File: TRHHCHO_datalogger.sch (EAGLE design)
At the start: 39 parts, among them J6 AMP FCI 10103594-0001LF, U1 ATMEGA328P-MU, U10 TSL2591, U2 FT231XQ-R, U3 DS3234, U7 SHT31/35, U8 MCP1703/3.3V, Y2 SPARKFUN_RESONATORSMD

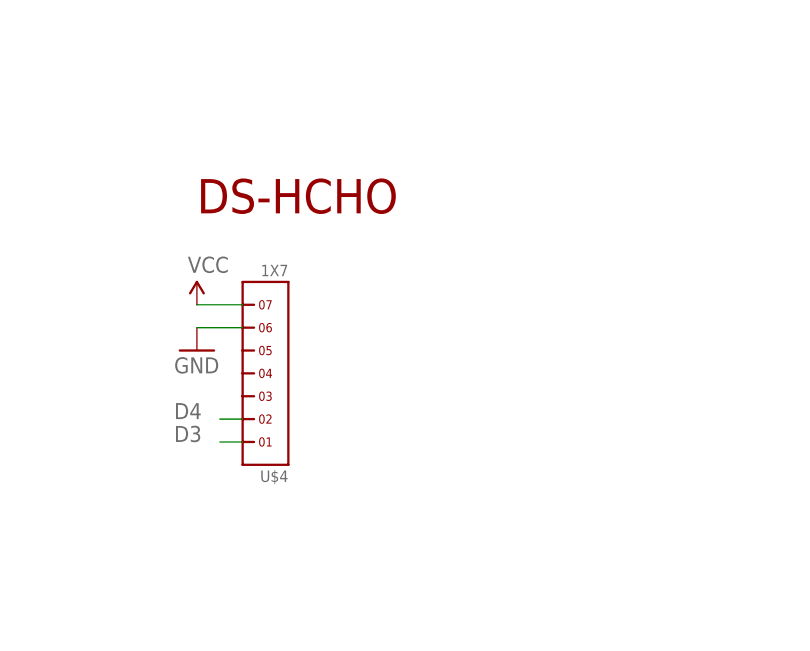
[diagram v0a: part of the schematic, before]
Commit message: Updated footprint of HCHO sensor
- Now using proper dimensions given by manufacturer
- Small trace adjustments
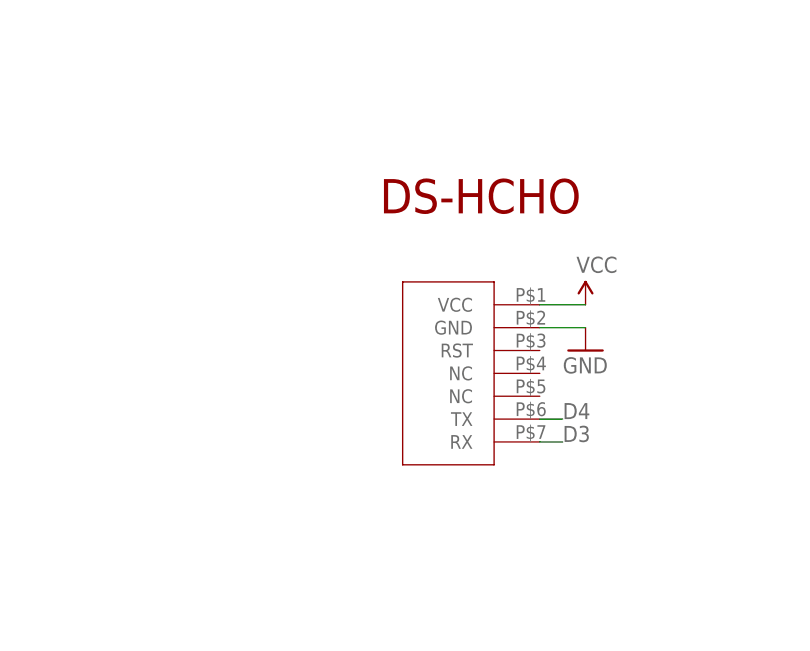
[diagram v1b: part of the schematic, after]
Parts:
- removed U$4: 1X7, headers(2mm):1X7
- added U$5: DS_HCHO, Plantower-DS-HCHO:DS_HCHO
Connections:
- net D3: now also U$5.RX; no longer U$4.1
- net D4: now also U$5.TX; no longer U$4.2
- net GND: now also U$5.GND; no longer U$4.6
- net VCC: now also U$5.VCC; no longer U$4.7
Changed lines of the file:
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@@
 </part>
 <part name="GND8" library="SparkFun-Aesthetics" deviceset="GND" device=""/>
-<part name="U8" library="linear" library_urn="urn:adsk.eagle:library:262" deviceset="MCP1703" device="CB" value="MCP1703/3.3V">
+<part name="U8" library="linear" library_urn="urn:adsk.eagle:library:262" deviceset="MCP1703" device="CB" package3d_urn="urn:adsk.eagle:package:16489/2" value="MCP1703/3.3V">
 <attribute name="MPN" value="MCP1703T-2502E/CB"/>
 </part>
@@
 <part name="J6" library="SparkFun-Connectors" deviceset="USB_MICRO-B" device="_HALF_PTH" value="AMP FCI 10103594-0001LF"/>
 <part name="GND11" library="SparkFun-Aesthetics" deviceset="GND" device=""/>
-<part name="U$4" library="headers(2mm)" deviceset="1X7" device=""/>
-<part name="SUPPLY6" library="SparkFun-Aesthetics" deviceset="VCC" device=""/>
-<part name="GND9" library="SparkFun-Aesthetics" deviceset="GND" device=""/>
 <part name="U10" library="TSL2591" deviceset="LIGHT_TSL2591" device="" value="TSL2591">
 <attribute name="MPN" value="TSL25911FN "/>
@@
 <attribute name="MPN" value="GRM155R71C104KA88J"/>
 </part>
+<part name="U$5" library="Plantower-DS-HCHO" deviceset="DS_HCHO" device=""/>
+<part name="SUPPLY9" library="SparkFun-Aesthetics" deviceset="VCC" device=""/>
+<part name="GND13" library="SparkFun-Aesthetics" deviceset="GND" device=""/>
 </parts>
 <sheets>
@@
 <text x="212.598" y="-109.728" size="2.1844" layer="94" font="vector" ratio="15">SENSORS</text>
 <text x="241.3" y="-60.96" size="3.81" layer="94">TagConnect ISP</text>
-<text x="104.14" y="22.86" size="3.81" layer="94">DS-HCHO</text>
+<text x="124.46" y="22.86" size="3.81" layer="94">DS-HCHO</text>
 <text x="71.12" y="-48.26" size="2.54" layer="94" font="vector">Light Intensity</text>
 <text x="93.98" y="-76.2" size="1.778" layer="97">0x29</text>
@@
 </instance>
 <instance part="GND11" gate="1" x="-48.26" y="78.74"/>
-<instance part="U$4" gate="G$1" x="111.76" y="5.08" rot="R180"/>
-<instance part="SUPPLY6" gate="G$1" x="104.14" y="12.7"/>
-<instance part="GND9" gate="1" x="104.14" y="7.62"/>
 <instance part="U10" gate="G$1" x="93.98" y="-63.5">
 <attribute name="MPN" x="93.98" y="-63.5" size="1.778" layer="96" display="off"/>
@@
 <attribute name="MPN" x="71.12" y="-66.04" size="1.778" layer="96" rot="R180" display="off"/>
 </instance>
+<instance part="U$5" gate="G$1" x="132.08" y="-5.08"/>
+<instance part="SUPPLY9" gate="G$1" x="147.32" y="12.7"/>
+<instance part="GND13" gate="1" x="147.32" y="7.62"/>
 </instances>
 <busses>
@@
 </segment>
 <segment>
-<pinref part="U$4" gate="G$1" pin="6"/>
-<wire x1="109.22" y1="10.16" x2="104.14" y2="10.16" width="0.1524" layer="91"/>
-<pinref part="GND9" gate="1" pin="GND"/>
-</segment>
-<segment>
 <pinref part="C4" gate="G$1" pin="1"/>
 <wire x1="71.12" y1="-71.12" x2="71.12" y2="-73.66" width="0.1524" layer="91"/>
@@
 <wire x1="78.74" y1="-71.12" x2="71.12" y2="-71.12" width="0.1524" layer="91" style="longdash"/>
 <junction x="71.12" y="-71.12"/>
+</segment>
+<segment>
+<pinref part="U$5" gate="G$1" pin="GND"/>
+<wire x1="142.24" y1="10.16" x2="147.32" y2="10.16" width="0.1524" layer="91"/>
+<pinref part="GND13" gate="1" pin="GND"/>
 </segment>
 </net>
@@
 </segment>
 <segment>
-<pinref part="U$4" gate="G$1" pin="7"/>
-<wire x1="109.22" y1="12.7" x2="104.14" y2="12.7" width="0.1524" layer="91"/>
-<pinref part="SUPPLY6" gate="G$1" pin="VCC"/>
-</segment>
-<segment>
 <label x="78.74" y="-68.58" size="1.778" layer="95"/>
 <wire x1="71.12" y1="-63.5" x2="71.12" y2="-60.96" width="0.1524" layer="91"/>
@@
 <wire x1="76.2" y1="-63.5" x2="71.12" y2="-63.5" width="0.1524" layer="91" style="longdash"/>
 <junction x="71.12" y="-63.5"/>
+</segment>
+<segment>
+<pinref part="U$5" gate="G$1" pin="VCC"/>
+<wire x1="142.24" y1="12.7" x2="147.32" y2="12.7" width="0.1524" layer="91"/>
+<pinref part="SUPPLY9" gate="G$1" pin="VCC"/>
 </segment>
 </net>
@@
 </segment>
 <segment>
-<pinref part="U$4" gate="G$1" pin="1"/>
-<wire x1="109.22" y1="-2.54" x2="106.68" y2="-2.54" width="0.1524" layer="91"/>
-<label x="101.6" y="-2.54" size="1.778" layer="95"/>
+<pinref part="U$5" gate="G$1" pin="RX"/>
+<wire x1="142.24" y1="-2.54" x2="144.78" y2="-2.54" width="0.1524" layer="91"/>
+<label x="144.78" y="-2.54" size="1.778" layer="95"/>
 </segment>
 </net>
@@
 </segment>
 <segment>
-<pinref part="U$4" gate="G$1" pin="2"/>
-<wire x1="109.22" y1="0" x2="106.68" y2="0" width="0.1524" layer="91"/>
-<label x="101.6" y="0" size="1.778" layer="95"/>
+<pinref part="U$5" gate="G$1" pin="TX"/>
+<wire x1="142.24" y1="0" x2="144.78" y2="0" width="0.1524" layer="91"/>
+<label x="144.78" y="0" size="1.778" layer="95"/>
 </segment>
 </net>
@@
 with this version.
 </note>
+<note version="8.3" severity="warning">
+Since Version 8.3, EAGLE supports URNs for individual library
+assets (packages, symbols, and devices). The URNs of those assets
+will not be understood (or retained) with this version.
+</note>
+<note version="8.3" severity="warning">
+Since Version 8.3, EAGLE supports the association of 3D packages
+with devices in libraries, schematics, and board files. Those 3D
+packages will not be understood (or retained) with this version.
+</note>
 </compatibility>
